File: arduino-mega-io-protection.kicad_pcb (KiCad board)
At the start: 4 copper layers, 150.1 x 72 mm, 140 parts, among them J101 CONN_01X02, J102 CONN_01X02, J103 CONN_01X02, J104 CONN_01X02, J105 CONN_01X02, J106 CONN_01X02, J107 CONN_01X02, J108 CONN_01X36, J109 CONN_01X10, J110 CONN_02X18, J111 CONN_01X08, J112 CONN_01X08, J113 CONN_01X08, J114 CONN_01X08, J115 CONN_01X08, U201 MOCD217M, U202 MOCD217M, U203 MOCD217M, U204 MOCD217M, U205 MOCD217M, U206 MOCD217M, U207 MOCD217M, U208 MOCD217M, U209 MOCD217M, U210 MOCD217M, U211 MOCD217M, U212 MOCD217M, U213 MOCD217M, U214 MOCD217M, U215 MOCD217M, U216 MOCD217M, U217 MOCD217M, U218 MOCD217M, U219 MOCD217M, U220 MOCD217M, U221 MOCD217M, U222 MOCD217M

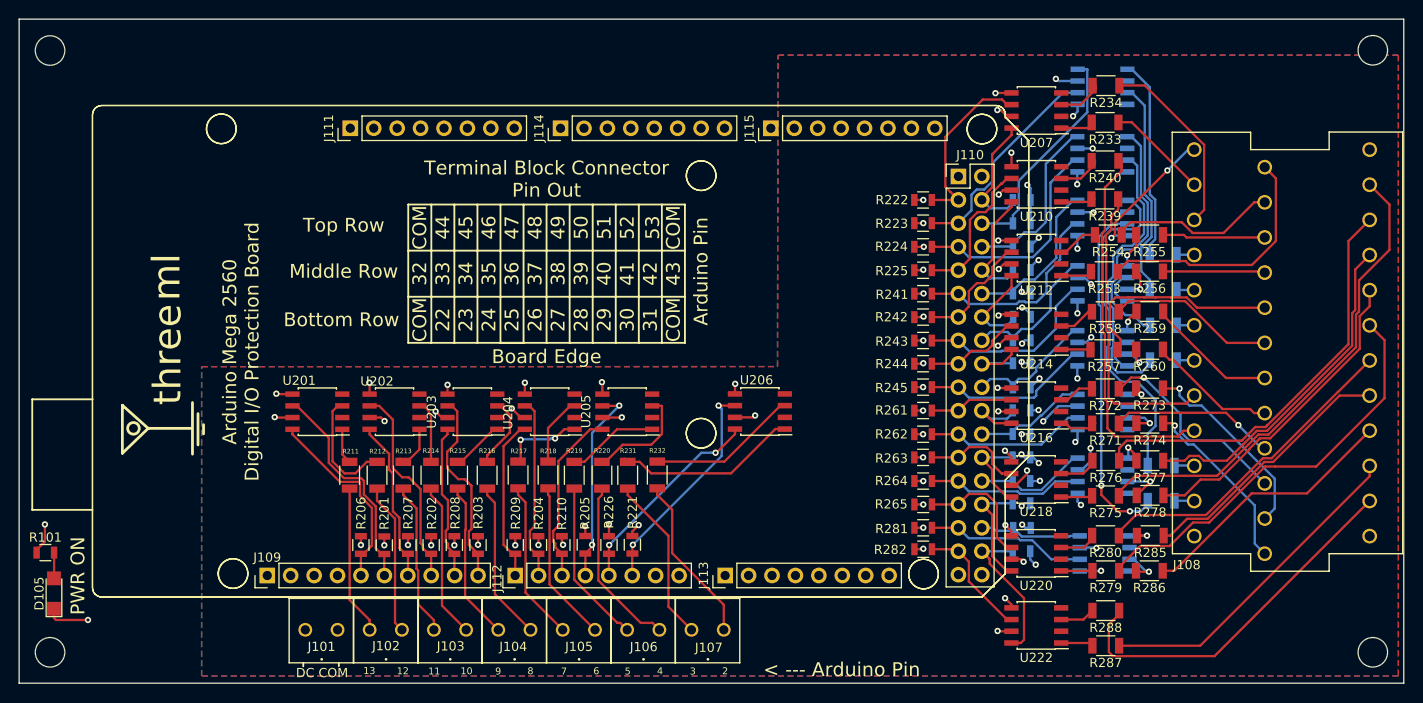
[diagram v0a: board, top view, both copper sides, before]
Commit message: footprints cleaned-up and submitted to oshpark!
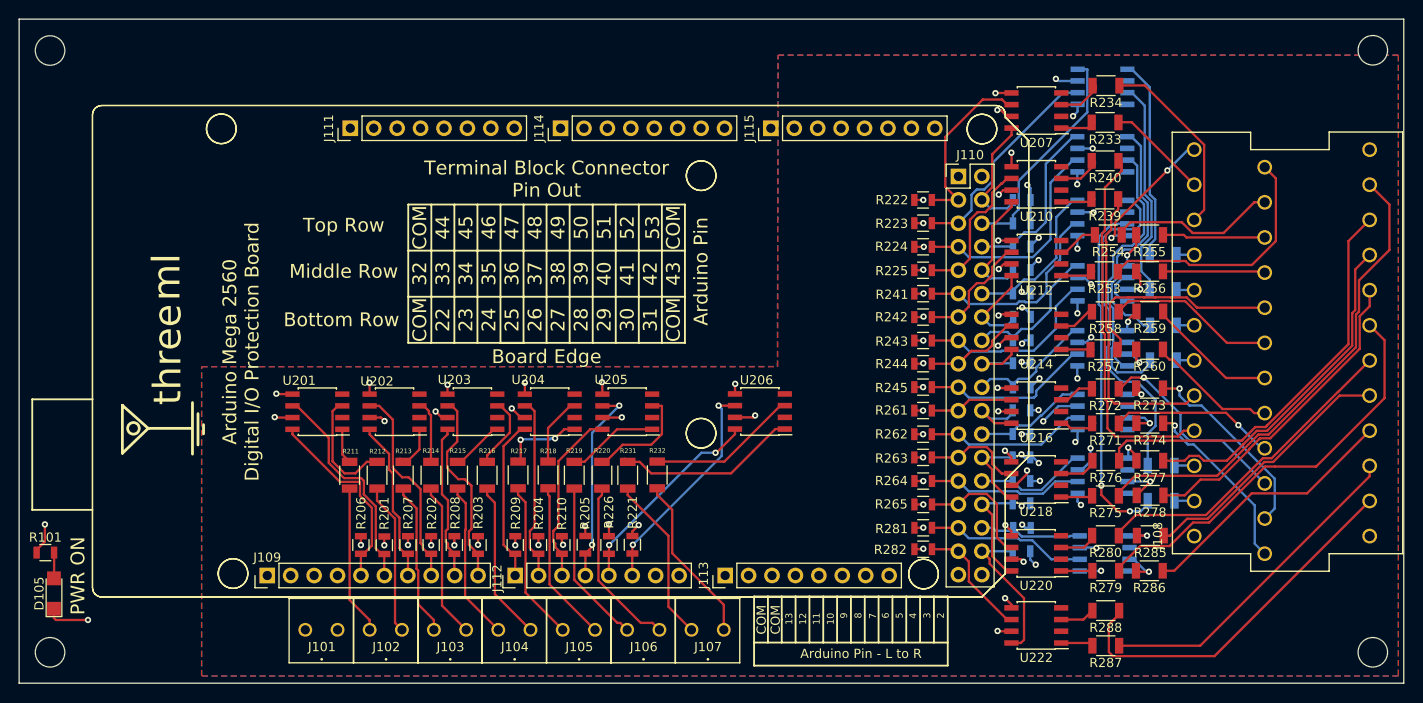
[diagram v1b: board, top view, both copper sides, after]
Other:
- rule pad_to_mask_clearance: 0.2 -> 0.0254
- board text added: "Arduino Pin - L to R"
- board text removed: "< --- Arduino Pin"
- board text removed: "DC COM"

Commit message: adding serial 1, 2, and 3 as protected inputs
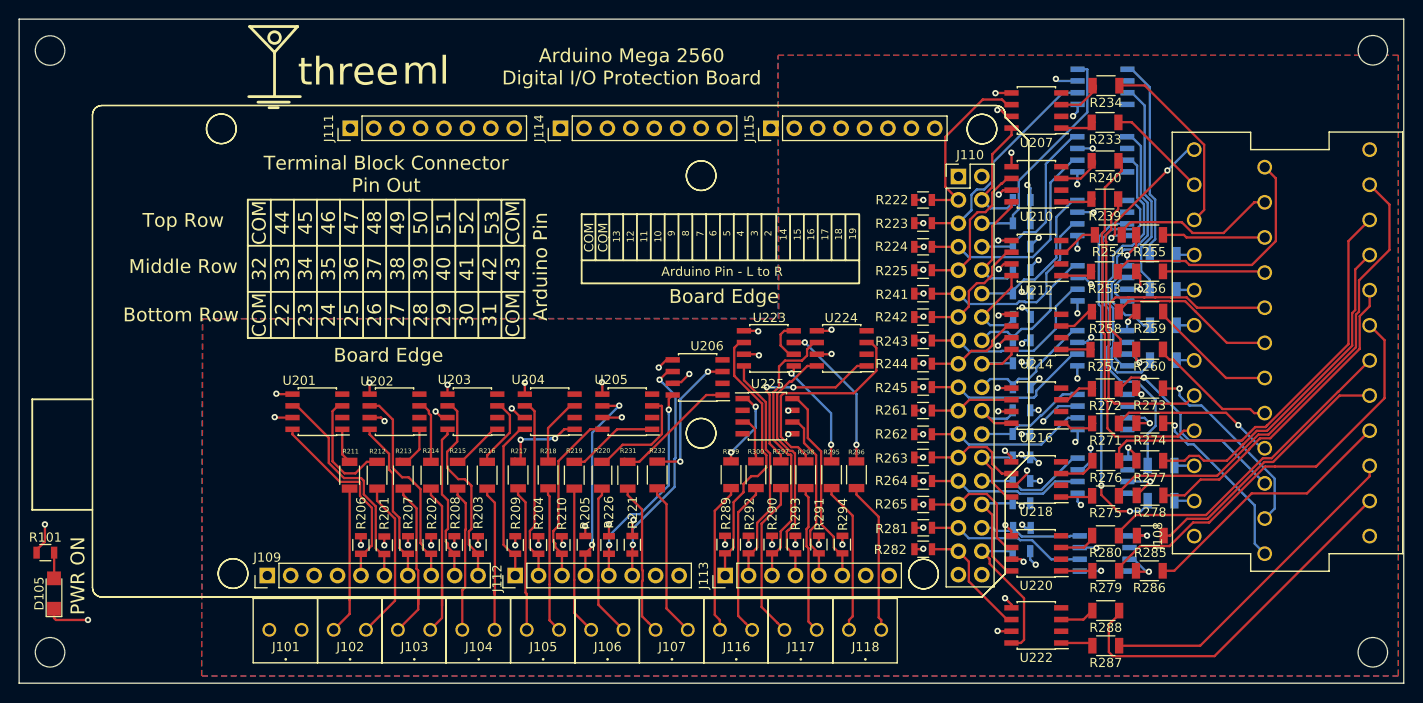
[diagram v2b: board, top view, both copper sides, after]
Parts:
- added J116: CONN_01X02, 3ML_Footprint_Library:Wurth_691103010002, F.Cu at (150.4, 140.0)
- added J117: CONN_01X02, 3ML_Footprint_Library:Wurth_691103010002, F.Cu at (157.4, 140.0)
- added J118: CONN_01X02, 3ML_Footprint_Library:Wurth_691103010002, F.Cu at (164.4, 140.0)
- added R289: 10K, Resistors_SMD:R_0805, F.Cu at (151.0, 130.8)
- added R290: 10K, Resistors_SMD:R_0805, F.Cu at (156.1, 130.8)
- added R291: 10K, Resistors_SMD:R_0805, F.Cu at (161.2, 130.8)
- added R292: 10K, Resistors_SMD:R_0805, F.Cu at (153.5, 130.8)
- added R293: 10K, Resistors_SMD:R_0805, F.Cu at (158.6, 130.8)
- added R294: 10K, Resistors_SMD:R_0805, F.Cu at (163.7, 130.8)
- added R295: 4.8k, Resistors_SMD:R_1206, F.Cu at (162.5, 123.2)
- added R296: 4.8k, Resistors_SMD:R_1206, F.Cu at (165.2, 123.2)
- added R297: 4.8k, Resistors_SMD:R_1206, F.Cu at (157.0, 123.2)
- added R298: 4.8k, Resistors_SMD:R_1206, F.Cu at (159.7, 123.2)
- added R299: 4.8k, Resistors_SMD:R_1206, F.Cu at (151.6, 123.2)
- added R300: 4.8k, Resistors_SMD:R_1206, F.Cu at (154.3, 123.2)
- added U223: MOCD217M, Housings_SOIC:SOIC-8_3.9x4.9mm_Pitch1.27mm, F.Cu at (155.7, 109.5)
- added U224: MOCD217M, Housings_SOIC:SOIC-8_3.9x4.9mm_Pitch1.27mm, F.Cu at (163.6, 109.5)
- added U225: MOCD217M, Housings_SOIC:SOIC-8_3.9x4.9mm_Pitch1.27mm, F.Cu at (155.6, 116.9)
- moved ACC106 37.1 mm to (102.1, 82.2), turned to 0 degrees
- moved U206 7.70 mm to (148.0, 112.7)
- moved J103 3.90 mm to (115.5, 140.0)
- moved J104 3.90 mm to (122.5, 140.0)
- moved J106 3.90 mm to (136.5, 140.0)
- moved J101 3.90 mm to (101.6, 140.0)
- moved J102 3.90 mm to (108.6, 140.0)
- moved J105 3.90 mm to (129.5, 140.0)
- moved J107 3.90 mm to (143.5, 140.0)
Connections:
- J113 pad 1: (no net) -> /DIN14
- J113 pad 2: (no net) -> /DIN15
- J113 pad 3: (no net) -> /DIN16
- J113 pad 4: (no net) -> /DIN17
- J113 pad 5: (no net) -> /DIN18
- J113 pad 6: (no net) -> /DIN19
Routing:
- net /DIN16: track 0.00 -> 30.5 mm
- net /DIN14: track 0.00 -> 30.3 mm
- net /DIN17: track 0.00 -> 27.2 mm
- net /DIN15: track 0.00 -> 25.0 mm
- net Net-(R298-Pad2): track 0.00 -> 23.9 mm
- net /DIN19: track 0.00 -> 21.9 mm
- net Net-(R297-Pad2): track 0.00 -> 20.5 mm, vias 0 -> 2
- net /DIN18: track 0.00 -> 18.5 mm
- net /F_DIN17: track 0.00 -> 17.3 mm
- net /F_DIN18: track 0.00 -> 16.8 mm
- net /F_DIN15: track 0.00 -> 16.5 mm
- net /F_DIN14: track 0.00 -> 16.5 mm
- net Net-(R296-Pad2): track 0.00 -> 16.4 mm, vias 0 -> 2
- net /F_DIN19: track 0.00 -> 16.3 mm
- net /F_DIN16: track 0.00 -> 16.0 mm
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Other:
- board text added: "14"
- board text added: "15"
- board text added: "16"
- board text added: "17"
- board text added: "18"
- board text added: "19"
